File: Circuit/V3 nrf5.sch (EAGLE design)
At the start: 54 parts, among them J4 USB Micro, J7 CORTEX_DEBUG_SMD, Q2 BSS84, U1 74AHCT2G125, U2 MCP73831, U3 BC840M, U4 MIC5205, U8 TPS61235P, Y1 32.768kHz

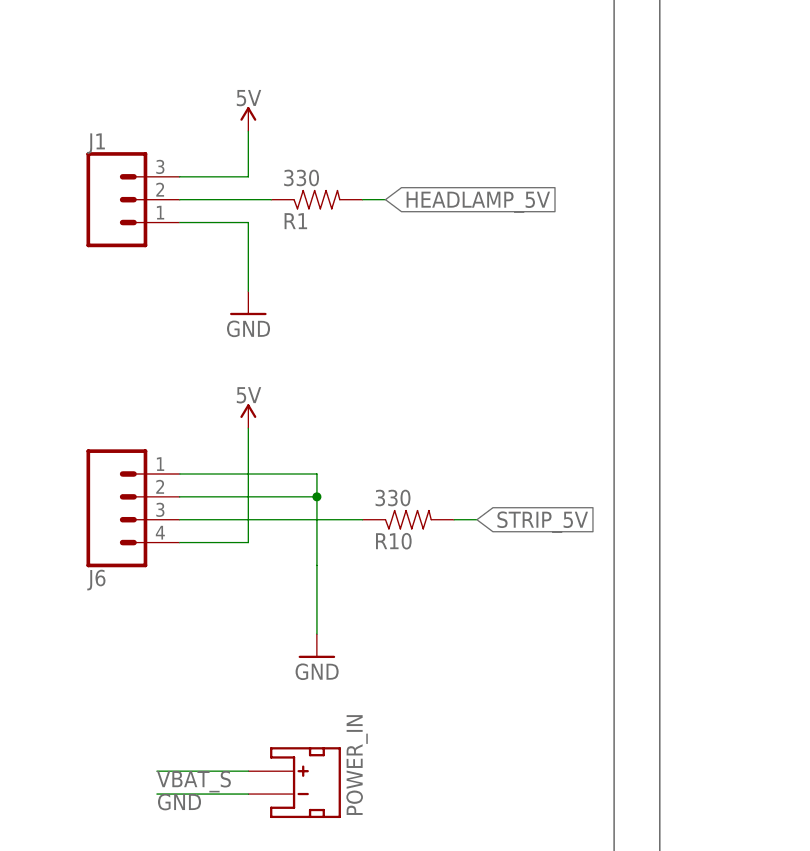
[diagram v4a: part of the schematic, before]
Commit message: Moving from millis timealive to seconds timealive.
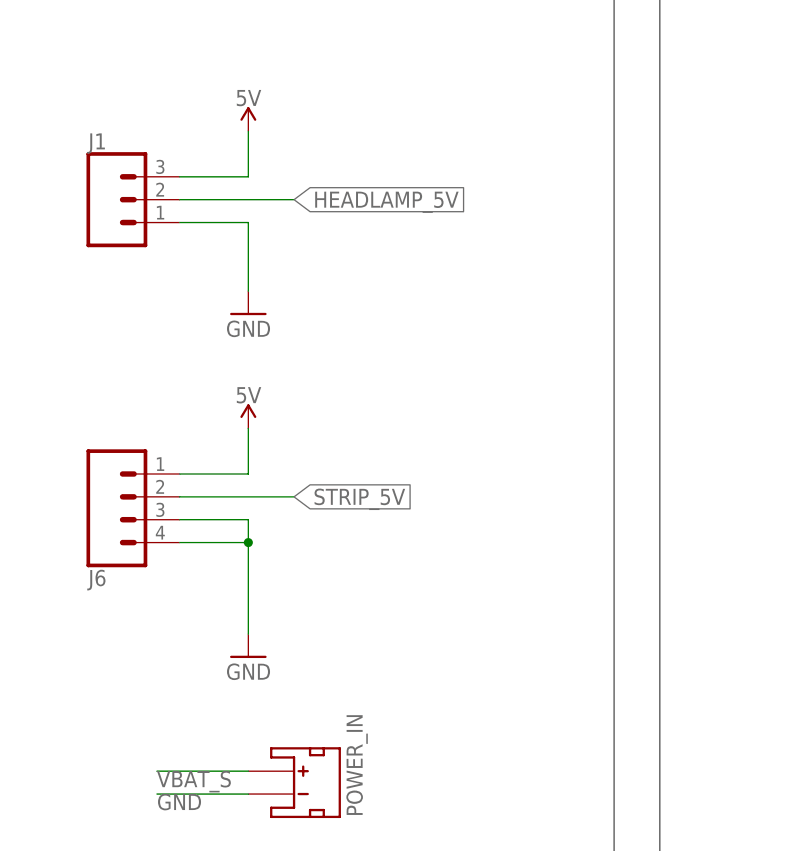
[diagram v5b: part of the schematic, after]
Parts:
- removed R1, R10: 330, SparkFun:RESISTOR0603-RES
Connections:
- removed net N$17: J1.2, R1.1
- removed net N$2: J6.3, R10.1
- net 5V: now also J6.1; no longer J6.4
- net HEADLAMP_5V: now also J1.2; no longer R1.2
- net N$9: now also J6.3, J6.4; no longer J6.1, J6.2
- net STRIP_5V: now also J6.2; no longer R10.2
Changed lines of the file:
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@@
 <drawing>
 <settings>
-<setting alwaysvectorfont="no"/>
+<setting alwaysvectorfont="yes"/>
 <setting keepoldvectorfont="yes"/>
 <setting verticaltext="up"/>
@@
 <attribute name="DIGIKEY" value="277-1860-ND"/>
 </part>
-<part name="R10" library="SparkFun" deviceset="RESISTOR" device="0603-RES" value="330">
-<attribute name="DIGIKEY" value="P330HCT-ND"/>
-</part>
 <part name="GND18" library="SparkFun" deviceset="GND" device=""/>
 <part name="J7" library="SparkFun-Connectors" library_urn="urn:adsk.eagle:library:513" deviceset="CORTEX_DEBUG" device="_SMD" package3d_urn="urn:adsk.eagle:package:38289/1">
@@
 </part>
 <part name="GND4" library="SparkFun" deviceset="GND" device=""/>
-<part name="R1" library="SparkFun" deviceset="RESISTOR" device="0603-RES" value="330">
-<attribute name="DIGIKEY" value="P330HCT-ND"/>
-</part>
 <part name="P+10" library="SparkFun-PowerSymbols" deviceset="VCC" device="" value="5V"/>
 <part name="P+11" library="SparkFun" deviceset="3.3V" device="" value="VBAT"/>
@@
 </instance>
 <instance part="P+4" gate="G$1" x="144.78" y="167.64" smashed="yes"/>
-<instance part="GND2" gate="1" x="-38.1" y="66.04" smashed="yes" rot="MR0">
-<attribute name="VALUE" x="-35.56" y="63.5" size="1.778" layer="96" rot="MR0"/>
+<instance part="GND2" gate="1" x="-45.72" y="66.04" smashed="yes" rot="MR0">
+<attribute name="VALUE" x="-43.18" y="63.5" size="1.778" layer="96" rot="MR0"/>
 </instance>
 <instance part="R4" gate="G$1" x="-55.88" y="22.86" smashed="yes">
@@
 <attribute name="NAME" x="-63.5" y="75.692" size="1.778" layer="95" font="vector" rot="MR180"/>
 <attribute name="DIGIKEY" x="-58.42" y="83.82" size="3.4798" layer="96" ratio="10" rot="MR180" display="off"/>
-</instance>
-<instance part="R10" gate="G$1" x="-27.94" y="81.28" smashed="yes" rot="MR180">
-<attribute name="NAME" x="-31.75" y="79.7814" size="1.778" layer="95" rot="MR180"/>
-<attribute name="VALUE" x="-31.75" y="84.582" size="1.778" layer="96" rot="MR180"/>
-<attribute name="DIGIKEY" x="-27.94" y="81.28" size="3.4798" layer="96" ratio="10" rot="MR180" display="off"/>
 </instance>
 <instance part="GND18" gate="1" x="137.668" y="81.28" smashed="yes">
@@
 <instance part="GND4" gate="1" x="-45.72" y="104.14" smashed="yes" rot="MR0">
 <attribute name="VALUE" x="-43.18" y="101.6" size="1.778" layer="96" rot="MR0"/>
-</instance>
-<instance part="R1" gate="G$1" x="-38.1" y="116.84" smashed="yes" rot="MR180">
-<attribute name="NAME" x="-41.91" y="115.3414" size="1.778" layer="95" rot="MR180"/>
-<attribute name="VALUE" x="-41.91" y="120.142" size="1.778" layer="96" rot="MR180"/>
-<attribute name="DIGIKEY" x="-38.1" y="116.84" size="3.4798" layer="96" ratio="10" rot="MR180" display="off"/>
 </instance>
 <instance part="P+10" gate="G$1" x="-45.72" y="124.46" smashed="yes" rot="MR0">
@@
 <net name="STRIP_5V" class="0">
 <segment>
-<pinref part="R10" gate="G$1" pin="2"/>
-<wire x1="-22.86" y1="81.28" x2="-20.32" y2="81.28" width="0.1524" layer="91"/>
-<label x="-20.32" y="81.28" size="1.778" layer="95" rot="MR180" xref="yes"/>
+<wire x1="-53.34" y1="83.82" x2="-40.64" y2="83.82" width="0.1524" layer="91"/>
+<label x="-40.64" y="83.82" size="1.778" layer="95" rot="MR180" xref="yes"/>
+<pinref part="J6" gate="G$1" pin="2"/>
 </segment>
 <segment>
@@
 <segment>
 <pinref part="P+14" gate="G$1" pin="VCC"/>
-<pinref part="J6" gate="G$1" pin="4"/>
-<wire x1="-53.34" y1="78.74" x2="-45.72" y2="78.74" width="0.1524" layer="91"/>
-<wire x1="-45.72" y1="78.74" x2="-45.72" y2="91.44" width="0.1524" layer="91"/>
+<wire x1="-45.72" y1="91.44" x2="-45.72" y2="86.36" width="0.1524" layer="91"/>
+<pinref part="J6" gate="G$1" pin="1"/>
+<wire x1="-45.72" y1="86.36" x2="-53.34" y2="86.36" width="0.1524" layer="91"/>
 </segment>
 <segment>
@@
 <net name="HEADLAMP_5V" class="0">
 <segment>
-<pinref part="R1" gate="G$1" pin="2"/>
-<wire x1="-33.02" y1="116.84" x2="-30.48" y2="116.84" width="0.1524" layer="91"/>
-<label x="-30.48" y="116.84" size="1.778" layer="95" rot="MR180" xref="yes"/>
+<label x="-40.64" y="116.84" size="1.778" layer="95" rot="MR180" xref="yes"/>
+<pinref part="J1" gate="J$1" pin="2"/>
+<wire x1="-53.34" y1="116.84" x2="-40.64" y2="116.84" width="0.1524" layer="91"/>
 </segment>
 <segment>
@@
 </segment>
 </net>
-<net name="N$17" class="0">
-<segment>
-<pinref part="R1" gate="G$1" pin="1"/>
-<wire x1="-53.34" y1="116.84" x2="-43.18" y2="116.84" width="0.1524" layer="91"/>
-<pinref part="J1" gate="J$1" pin="2"/>
-</segment>
-</net>
 <net name="N$9" class="0">
 <segment>
-<pinref part="J6" gate="G$1" pin="2"/>
-<wire x1="-53.34" y1="83.82" x2="-38.1" y2="83.82" width="0.1524" layer="91"/>
-<wire x1="-38.1" y1="83.82" x2="-38.1" y2="86.36" width="0.1524" layer="91"/>
-<pinref part="J6" gate="G$1" pin="1"/>
-<wire x1="-53.34" y1="86.36" x2="-38.1" y2="86.36" width="0.1524" layer="91"/>
-<wire x1="-38.1" y1="83.82" x2="-38.1" y2="76.2" width="0.1524" layer="91"/>
-<junction x="-38.1" y="83.82"/>
 <pinref part="GND2" gate="1" pin="GND"/>
-<wire x1="-38.1" y1="76.2" x2="-38.1" y2="68.58" width="0.1524" layer="91"/>
-</segment>
-</net>
-<net name="N$2" class="0">
-<segment>
+<wire x1="-45.72" y1="68.58" x2="-45.72" y2="78.74" width="0.1524" layer="91"/>
 <pinref part="J6" gate="G$1" pin="3"/>
-<pinref part="R10" gate="G$1" pin="1"/>
-<wire x1="-53.34" y1="81.28" x2="-33.02" y2="81.28" width="0.1524" layer="91"/>
-</segment>
-</net>
+<wire x1="-45.72" y1="78.74" x2="-45.72" y2="81.28" width="0.1524" layer="91"/>
+<wire x1="-45.72" y1="81.28" x2="-53.34" y2="81.28" width="0.1524" layer="91"/>
+<pinref part="J6" gate="G$1" pin="4"/>
+<wire x1="-53.34" y1="78.74" x2="-45.72" y2="78.74" width="0.1524" layer="91"/>
+<junction x="-45.72" y="78.74"/>
+</segment>
+</net>

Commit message: updated footprints level-shifter, cystral and connetors
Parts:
- removed U1: 74AHCT2G125, cdclvc11xx_10:74AHCT2G125
- removed Y1: 32.768kHz, SparkFun-Clocks:CRYSTAL-32.768KHZSMD-3.2X1.5
- added J2: (no value), SparkFun-Connectors:CONN_06SMD-1MM
- added J5: (no value), SparkFun-Connectors:CONN_04SMD2
- added U5: 74AHCT2G125, VSSOP8:VSSOP-8_DEVICE
- added Y2: (no value), SparkFun-Clocks:CRYSTAL-32.768KHZ
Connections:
- removed net N$10: C9.1, U3.F7/P001, Y1.2
- removed net N$8: C17.1, U3.F6/P000, Y1.1
- new net N$17: C17.1, U3.F6/P000, Y2.2
- new net N$2: C9.1, U3.F7/P001, Y2.1
- new net PIN_01: J2.3, U3.D1/P105
- new net PIN_02: J2.4, U3.E0/P103
- new net PIN_03: J2.5, U3.E1/P106
- new net PIN_04: J2.6, U3.F4/P002
- new net SCL: J5.4, U3.D6/P027
- new net SDA: J5.3, U3.E6/P026
- net 3.3V: now also J2.2, J5.2
- net 5V: now also U5.8; no longer U1.VCC
- net GND: now also J2.1, J5.1, U5.1, U5.4, U5.7; no longer U1.1!OE, U1.2!OE, U1.GND
- net HEADLAMP_3V3: now also U5.5; no longer U1.2A
- net HEADLAMP_5V: now also U5.3; no longer U1.2Y
- net STRIP_3V3: now also U5.2; no longer U1.1A
- net STRIP_5V: now also U5.6; no longer U1.1Y
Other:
- moved on the sheet: TP4, TP5

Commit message: V8 of the board, ready to print.
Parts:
- added S4: (no value), SparkFun-Switches:SWITCH-SPDT-PTH-11.6X4.0MM
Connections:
- removed net N$9: J6.3, J6.4
- removed net VBAT_S: C12.1, POWER_IN.+, S3.P, TP3.PP, U2.VBAT
- new net VBAT_RAW: C12.1, POWER_IN.+, S3.P, S4.P, TP3.PP, U2.VBAT
- net GND: now also J6.3, J6.4
- net VBAT: now also S4.O
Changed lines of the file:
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@@
 <drawing>
 <settings>
-<setting alwaysvectorfont="no"/>
+<setting alwaysvectorfont="yes"/>
 <setting keepoldvectorfont="yes"/>
 <setting verticaltext="up"/>
@@
 <part name="P+8" library="SparkFun" deviceset="3.3V" device="" value="3.3V"/>
 <part name="GND15" library="SparkFun" deviceset="GND" device=""/>
+<part name="S4" library="SparkFun-Switches" library_urn="urn:adsk.eagle:library:535" deviceset="SWITCH-SPDT" device="-PTH-11.6X4.0MM" package3d_urn="urn:adsk.eagle:package:40177/1"/>
 </parts>
 <sheets>
@@
 <attribute name="VALUE" x="30.48" y="12.7" size="1.778" layer="96"/>
 </instance>
+<instance part="S4" gate="1" x="449.58" y="144.78" smashed="yes">
+<attribute name="NAME" x="450.85" y="147.828" size="1.778" layer="95" font="vector" align="bottom-center"/>
+<attribute name="VALUE" x="450.596" y="141.478" size="1.778" layer="96" font="vector" align="top-center"/>
+</instance>
 </instances>
 <busses>
@@
 <pinref part="GND15" gate="1" pin="GND"/>
 <wire x1="33.02" y1="22.86" x2="33.02" y2="17.78" width="0.1524" layer="91"/>
+</segment>
+<segment>
+<pinref part="GND2" gate="1" pin="GND"/>
+<wire x1="-45.72" y1="68.58" x2="-45.72" y2="78.74" width="0.1524" layer="91"/>
+<pinref part="J6" gate="G$1" pin="3"/>
+<wire x1="-45.72" y1="78.74" x2="-45.72" y2="81.28" width="0.1524" layer="91"/>
+<wire x1="-45.72" y1="81.28" x2="-53.34" y2="81.28" width="0.1524" layer="91"/>
+<pinref part="J6" gate="G$1" pin="4"/>
+<wire x1="-53.34" y1="78.74" x2="-45.72" y2="78.74" width="0.1524" layer="91"/>
+<junction x="-45.72" y="78.74"/>
 </segment>
 </net>
@@
 <net name="VBAT" class="0">
 <segment>
-<pinref part="S3" gate="1" pin="O"/>
-<wire x1="454.66" y1="160.02" x2="457.2" y2="160.02" width="0.1524" layer="91"/>
-<label x="457.2" y="160.02" size="1.27" layer="95" xref="yes"/>
-</segment>
-<segment>
 <wire x1="370.84" y1="93.98" x2="373.38" y2="93.98" width="0.1524" layer="91"/>
 <pinref part="L4" gate="G$1" pin="2"/>
@@
 <pinref part="P+12" gate="G$1" pin="3.3V"/>
 </segment>
+<segment>
+<label x="462.28" y="160.02" size="1.778" layer="95"/>
+<wire x1="459.74" y1="160.02" x2="462.28" y2="160.02" width="0.1524" layer="91"/>
+<wire x1="459.74" y1="147.32" x2="459.74" y2="160.02" width="0.1524" layer="91"/>
+<pinref part="S4" gate="1" pin="O"/>
+<wire x1="459.74" y1="147.32" x2="454.66" y2="147.32" width="0.1524" layer="91"/>
+<pinref part="S3" gate="1" pin="O"/>
+<wire x1="454.66" y1="160.02" x2="459.74" y2="160.02" width="0.1524" layer="91"/>
+<junction x="459.74" y="160.02"/>
+</segment>
 </net>
 <net name="N$6" class="0">
@@
 </segment>
 </net>
-<net name="VBAT_S" class="0">
+<net name="VBAT_RAW" class="0">
 <segment>
 <label x="441.96" y="157.48" size="1.27" layer="95" rot="R90" xref="yes"/>
-<wire x1="447.04" y1="157.48" x2="441.96" y2="157.48" width="0.1524" layer="91"/>
+<wire x1="447.04" y1="157.48" x2="444.5" y2="157.48" width="0.1524" layer="91"/>
 <pinref part="S3" gate="1" pin="P"/>
+<pinref part="S4" gate="1" pin="P"/>
+<wire x1="444.5" y1="157.48" x2="441.96" y2="157.48" width="0.1524" layer="91"/>
+<wire x1="447.04" y1="144.78" x2="444.5" y2="144.78" width="0.1524" layer="91"/>
+<wire x1="444.5" y1="144.78" x2="444.5" y2="157.48" width="0.1524" layer="91"/>
+<junction x="444.5" y="157.48"/>
 </segment>
 <segment>
@@
 </segment>
 </net>
-<net name="N$9" class="0">
-<segment>
-<pinref part="GND2" gate="1" pin="GND"/>
-<wire x1="-45.72" y1="68.58" x2="-45.72" y2="78.74" width="0.1524" layer="91"/>
-<pinref part="J6" gate="G$1" pin="3"/>
-<wire x1="-45.72" y1="78.74" x2="-45.72" y2="81.28" width="0.1524" layer="91"/>
-<wire x1="-45.72" y1="81.28" x2="-53.34" y2="81.28" width="0.1524" layer="91"/>
-<pinref part="J6" gate="G$1" pin="4"/>
-<wire x1="-53.34" y1="78.74" x2="-45.72" y2="78.74" width="0.1524" layer="91"/>
-<junction x="-45.72" y="78.74"/>
-</segment>
-</net>

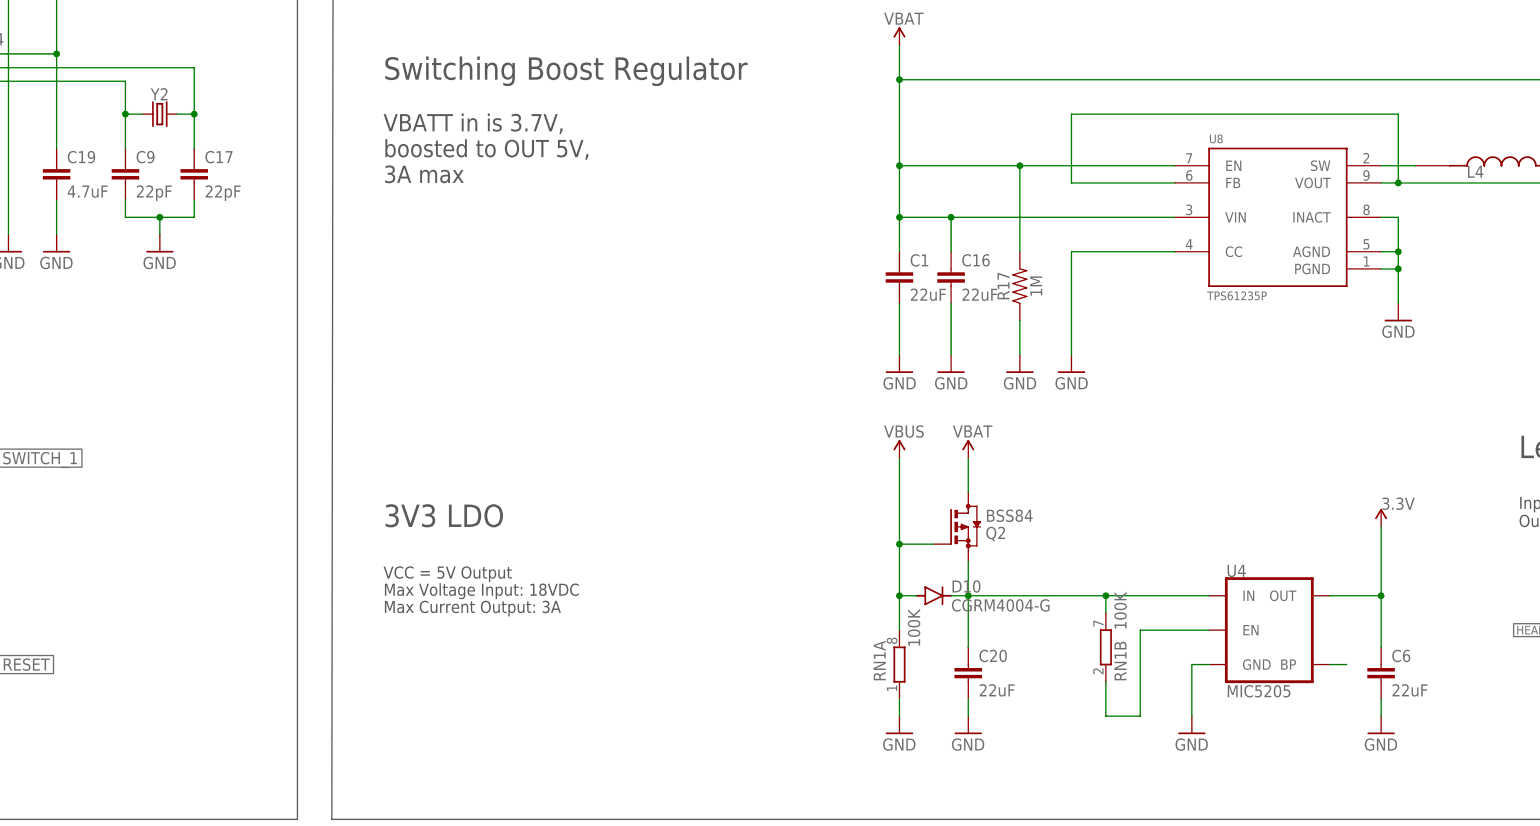
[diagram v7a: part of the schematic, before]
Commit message: Updating 10 components to different digikey values. A few changes, such as MIC5209 -> MIC5317.
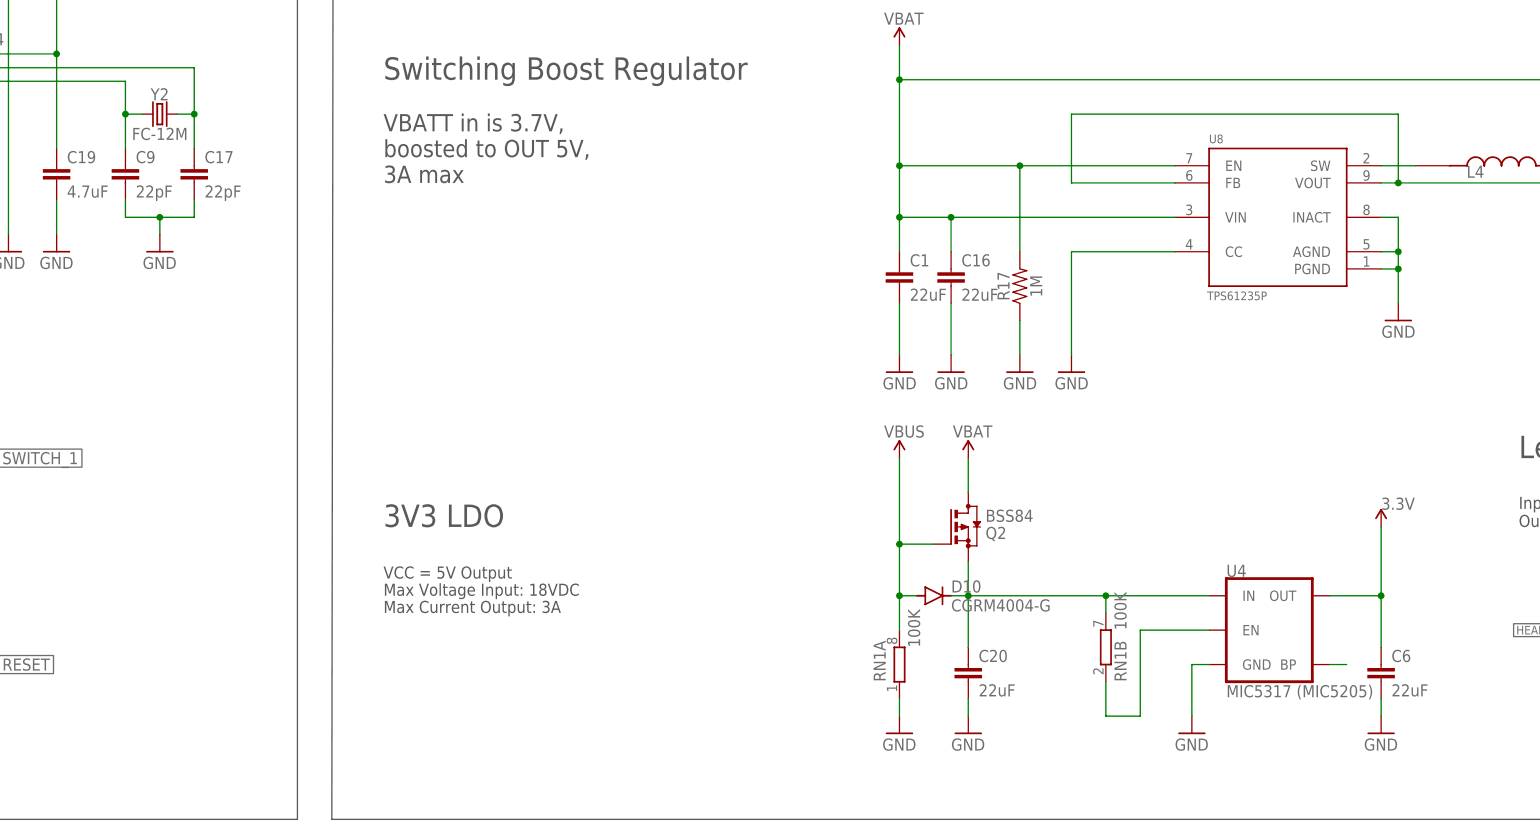
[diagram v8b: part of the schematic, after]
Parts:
- C1, C11: DIGIKEY 399-4925-1-ND -> 490-10511-1-ND
- C16, C6: DIGIKEY 399-8006-1-ND -> 490-10511-1-ND
- D3: DIGIKEY 160-1183-1-ND -> 754-1116-2-ND
- D7: DIGIKEY B340A-FDITR-ND -> MBRA340T3GOSTR-ND
- D8: DIGIKEY B340A-E3/61TGICT-ND -> MBRA340T3GOSTR-ND
- Q2: DIGIKEY DMG2305UX-13 -> DMP2120U-7DITR-ND
- R4, R6: DIGIKEY P330HCT-ND -> 311-330HRTR-ND
- U2: DIGIKEY MCP73831T-2ACI/OTCT-ND -> MCP73832T-2DFI/OTTR-ND
- U4: value MIC5205 -> MIC5317 (MIC5205); DIGIKEY 576-1259-1-ND -> MIC5317-3.3YM5-TR-ND
- Y2: value (none) -> FC-12M; device SparkFun-Clocks:CRYSTAL-32.768KHZ -> crystal:FC-12M; DIGIKEY (none) -> 2195-CM8V-T1A-32.768KHZ-12.5PF-20PPM-TA-QATR-ND
